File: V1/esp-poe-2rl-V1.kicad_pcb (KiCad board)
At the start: 2 copper layers, 88 x 45 mm, 94 parts, among them J1 USB_C_Receptacle_USB2.0, J2 RJ45 JACK, J3 1x2P 5,08mm, J4 1x2P 5,08mm, K1 G5NB-1A-E-DC5, K2 G5NB-1A-E-DC5, Q1 UMH3N, Q2 WPM2015-3/TR, Q3 LMUN2211LT1G, Q4 MMBT2222A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

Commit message: Prefab checks
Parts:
- D5, D7, D8: value GREEN -> EMERALD
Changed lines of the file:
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@@
 				(type "Bottom Solder Paste")
 			)
-			(layer "B.SilkS"
+			(layer "dielectric 2"
 				(type "Bottom Silk Screen")
+				(thickness 0)
+				(material "FR4")
+				(epsilon_r 4.5)
+				(loss_tangent 0.02)
 			)
 			(copper_finish "None")
@@
 			)
 		)
-		(property "Value" "GREEN"
+		(property "Value" "EMERALD"
 			(at 0 1.43 0)
 			(layer "F.Fab")
@@
 			)
 		)
-		(property "LCSC Part #" "C72043"
+		(property "LCSC Part #" "C2984266"
 			(at 0 0 0)
 			(layer "F.Fab")
@@
 			)
 		)
-		(property "Mfr" "Everlight"
+		(property "Mfr" "Everlight eLEC"
 			(at 0 0 0)
 			(layer "F.Fab")
@@
 			)
 		)
-		(property "Mfr PN" "19-217/GHC-YR1S2/3T"
+		(property "Mfr PN" "19-213/GHC-XS1T1/5T"
 			(at 0 0 0)
 			(layer "F.Fab")
@@
 			)
 		)
-		(property "Vendor PN" "C72043"
+		(property "Vendor PN" "C2984266"
 			(at 0 0 0)
 			(layer "F.Fab")
@@
 			)
 		)
-		(property "Value" "GREEN"
+		(property "Value" "EMERALD"
 			(at 0 1.43 0)
 			(layer "F.Fab")
@@
 			)
 		)
-		(property "LCSC Part #" "C72043"
+		(property "LCSC Part #" "C2984266"
 			(at 190.575 156 0)
 			(layer "F.Fab")
@@
 			)
 		)
-		(property "Mfr" "Everlight"
+		(property "Mfr" "Everlight eLEC"
 			(at 190.575 156 0)
 			(layer "F.Fab")
@@
 			)
 		)
-		(property "Mfr PN" "19-217/GHC-YR1S2/3T"
+		(property "Mfr PN" "19-213/GHC-XS1T1/5T"
 			(at 190.575 156 0)
 			(layer "F.Fab")
@@
 			)
 		)
-		(property "Vendor PN" "C72043"
+		(property "Vendor PN" "C2984266"
 			(at 190.575 156 0)
 			(layer "F.Fab")
@@
 			)
 		)
-		(property "Value" "GREEN"
+		(property "Value" "EMERALD"
 			(at 0 1.43 0)
 			(layer "F.Fab")
@@
 			)
 		)
-		(property "LCSC Part #" "C72043"
+		(property "LCSC Part #" "C2984266"
 			(at 164.575 156 0)
 			(layer "F.Fab")
@@
 			)
 		)
-		(property "Mfr" "Everlight"
+		(property "Mfr" "Everlight eLEC"
 			(at 164.575 156 0)
 			(layer "F.Fab")
@@
 			)
 		)
-		(property "Mfr PN" "19-217/GHC-YR1S2/3T"
+		(property "Mfr PN" "19-213/GHC-XS1T1/5T"
 			(at 164.575 156 0)
 			(layer "F.Fab")
@@
 			)
 		)
-		(property "Vendor PN" "C72043"
+		(property "Vendor PN" "C2984266"
 			(at 164.575 156 0)
 			(layer "F.Fab")

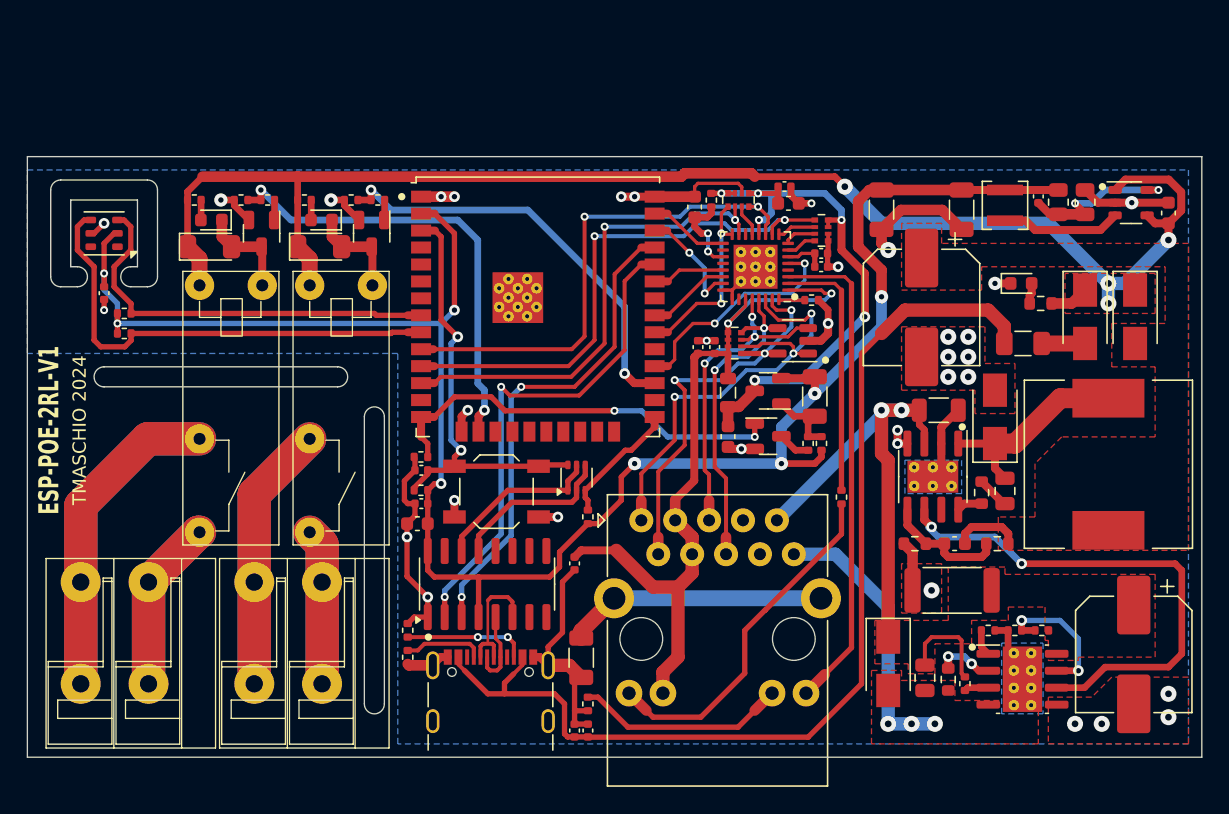
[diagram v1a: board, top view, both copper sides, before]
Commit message: Redoing routing because was too crapy
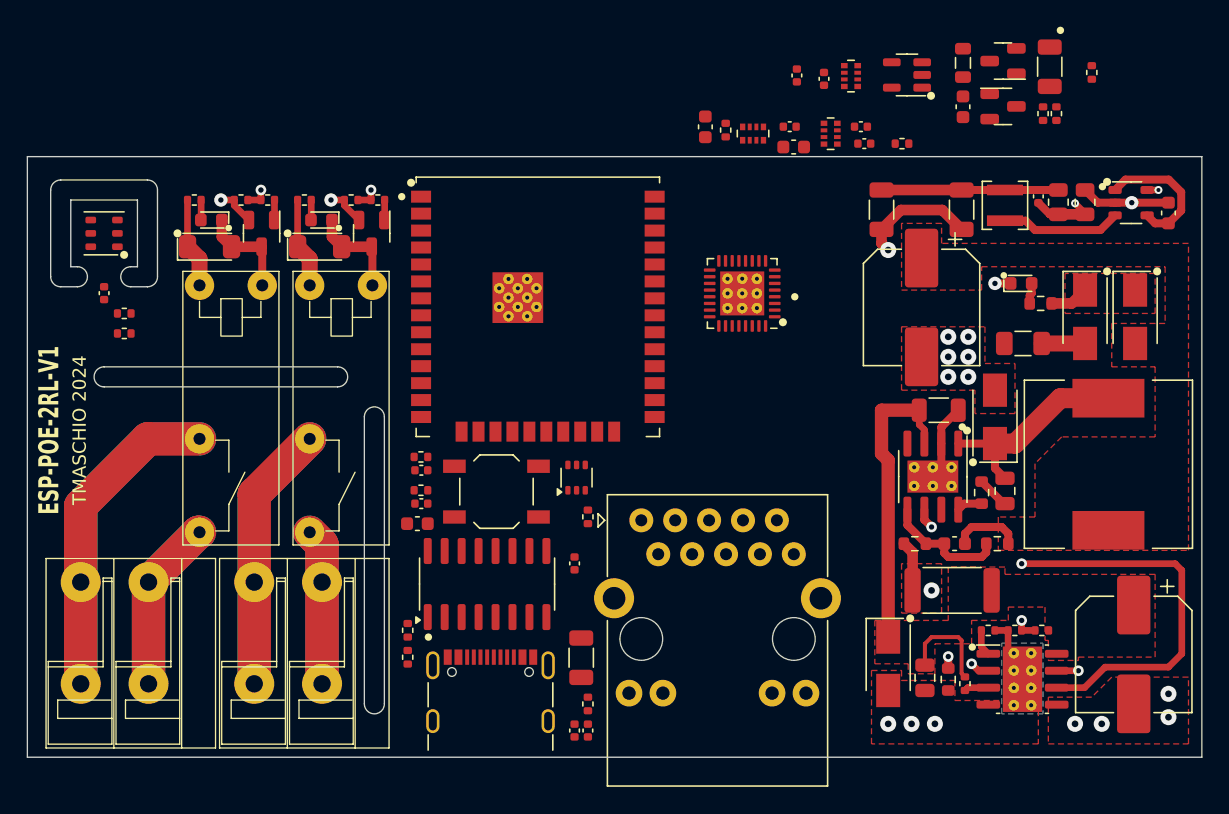
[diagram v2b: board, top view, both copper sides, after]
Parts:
- moved R21 36.9 mm to (155.8, 64.7)
- moved C24 30.3 mm to (152.6, 64.3)
- moved C25 30.3 mm to (146.1, 67.3)
- moved L3 30.3 mm to (146.1, 64.0)
- moved Q2 30.3 mm to (149.1, 63.8)
- moved Q3 30.3 mm to (149.1, 67.2)
- moved R23 30.3 mm to (153.1, 67.8)
- moved R24 30.3 mm to (152.1, 67.8)
- moved RN3 21.8 mm to (137.7, 65.0)
- moved C16 21.7 mm to (135.7, 65.2)
- moved D6 21.7 mm to (141.9, 64.9)
- moved C18 21.7 mm to (133.7, 64.9)
- moved R20 13.5 mm to (141.5, 70.0)
- moved C21 9.95 mm to (138.5, 68.8)
- moved C20 9.77 mm to (138.7, 70.0)
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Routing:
- net +3.3V: track 145.0 -> 13.2 mm, vias 8 -> 0
- net +5V: track 110.7 -> 26.7 mm, vias 4 -> 0
- net Net-(C10-Pad1): track 77.9 -> 0.00 mm
- net GND: track 100.1 -> 26.5 mm, vias 34 -> 16
- net +3.3VA: track 57.2 -> 0.00 mm, vias 2 -> 0
- net +3.3VLAN: track 43.7 -> 0.00 mm, vias 6 -> 0
- net /EMAC_RXD1: track 40.7 -> 0.00 mm, vias 2 -> 0
- net /EMAC_RXD0: track 38.1 -> 0.00 mm, vias 2 -> 0
- net Net-(U4-TXD): track 37.9 -> 0.00 mm, vias 2 -> 0
- net /LED_Y_A: track 37.1 -> 0.00 mm
- net Net-(U4-RXD): track 36.6 -> 0.00 mm, vias 2 -> 0
- net /EMAC_RX: track 36.3 -> 0.00 mm, vias 2 -> 0
- net I2C_SDA: track 35.7 -> 0.00 mm
- net /RD-: track 34.4 -> 0.00 mm, vias 3 -> 0
- net Net-(Q1A-C1): track 32.7 -> 0.00 mm, vias 2 -> 0
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- added copper zone on In1.Cu, net GND
- added copper zone on In1.Cu, net Net-(R7-Pad2)
- removed copper zone on B.Cu, net GND
- removed copper zone on B.Cu, net Net-(R7-Pad2)
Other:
- copper layers 2 -> 4

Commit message: Redoing routing
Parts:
- added R33: 22R/62,5mW, Tales:R_0402_1005Metric, F.Cu at (125.5, 86.5)
- moved RN3 29.5 mm to (134.5, 94.3), turned to 0 degrees
- moved RN2 14.5 mm to (133.3, 83.5), turned to 90 degrees
- moved RN1 14.2 mm to (130.3, 83.5)
- moved U6 7.65 mm to (131.1, 88.8)
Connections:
- U5 pad 28: /EMAC_CLK -> Net-(U5-IO17)
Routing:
- net /RD+: track 0.00 -> 17.9 mm, vias 0 -> 1
- net /RD-: track 0.00 -> 16.9 mm, vias 0 -> 3
- net /TD+: track 0.00 -> 15.1 mm, vias 0 -> 2
- net /TD-: track 0.00 -> 13.6 mm, vias 0 -> 2
- net /EMAC_MDIO: track 0.00 -> 6.57 mm
- net /EMAC_CLK: track 0.00 -> 4.21 mm
- net GND: track 26.5 -> 29.0 mm, vias 16 -> 18
- net +3.3VA: track 0.00 -> 1.56 mm
- net +3.3VLAN: track 0.00 -> 1.06 mm

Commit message: Update esp-poe-2rl-V1.kicad_pcb
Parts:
- moved R21 51.5 mm to (138.0, 113.0)
- moved D6 29.5 mm to (136.6, 94.0), turned to 0 degrees
- moved C16 28.3 mm to (126.8, 92.0), turned to 180 degrees
- moved C18 25.9 mm to (135.2, 90.8), turned to 0 degrees
- moved R20 22.6 mm to (135.3, 91.8)
- moved L3 21.5 mm to (128.0, 75.6), turned to -90 degrees
- moved C15 20.2 mm to (126.2, 89.0), turned to 0 degrees
- moved Q2 19.3 mm to (133.0, 74.5)
- moved Q3 19.1 mm to (133.0, 77.5)
- moved R22 19.0 mm to (137.0, 113.0), turned to 90 degrees
- moved R19 18.8 mm to (126.5, 87.8), turned to 180 degrees
- moved R23 18.7 mm to (135.5, 74.0), turned to -90 degrees
- moved R24 18.5 mm to (135.5, 76.0)
- moved C24 18.5 mm to (137.5, 75.0)
- moved C25 18.0 mm to (130.0, 75.3)
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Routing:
- net /LED_G_K: track 0.00 -> 28.1 mm, vias 0 -> 2
- net /LED_Y_A: track 0.00 -> 27.7 mm, vias 0 -> 1
- net /EMAC_CLK: track 4.21 -> 27.2 mm
- net PoE-: track 4.23 -> 26.5 mm
- net +3.3VA: track 1.56 -> 21.0 mm
- net Net-(J2-RLED-): track 0.00 -> 19.4 mm
- net Net-(J2-SHIELD): track 0.00 -> 15.5 mm
- net PoE+: track 30.2 -> 42.7 mm, vias 0 -> 3
- net /TD-: track 13.6 -> 25.5 mm, vias 2 -> 3
- net +3.3VLAN: track 1.06 -> 11.6 mm, vias 0 -> 3
- net /RD-: track 16.9 -> 24.0 mm, vias 3 -> 4
- net Net-(J2-LLED-): track 0.00 -> 6.15 mm
- net /RD+: track 17.9 -> 23.5 mm
- net /TD+: track 15.1 -> 20.6 mm
- net GND: track 29.0 -> 34.1 mm, vias 18 -> 21
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
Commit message: Redoing routing
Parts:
- SW1: footprint Tales:SW_SPST_TL3342 -> Tales:SW_SPST_Xunpu_TS1088AR02016
- moved C23 9.39 mm to (124.0, 95.2), turned to 180 degrees
- moved R17 9.19 mm to (124.8, 91.8)
- moved R15 9.01 mm to (113.5, 106.8), turned to 0 degrees
- moved R14 4.36 mm to (108.5, 106.8), turned to 180 degrees
- moved C12 2.85 mm to (106.0, 95.8)
- moved C13 2.50 mm to (105.5, 94.5)
- moved R16 2.50 mm to (107.5, 94.5), turned to 0 degrees
- moved C14 2.24 mm to (107.5, 93.5)
- moved C15 2.00 mm to (126.2, 87.0)
- moved C10 1.79 mm to (116.8, 112.2), turned to -90 degrees
- moved C11 1.79 mm to (117.8, 112.2), turned to -90 degrees
- moved SW1 1.39 mm to (112.0, 95.0), turned to 0 degrees
- moved U4 1.12 mm to (110.9, 102.0)
- moved R33 0.95 mm to (125.5, 85.8)
- moved R19 0.50 mm to (126.5, 88.2)
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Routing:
- net +3.3V: track 13.2 -> 89.5 mm, vias 0 -> 3
- net +3.3VA: track 21.0 -> 47.1 mm, vias 0 -> 1
- net Net-(C10-Pad1): track 0.00 -> 12.8 mm
- net Net-(Q1A-E1): track 0.00 -> 12.3 mm
- net Net-(Q1A-B1): track 0.00 -> 11.8 mm
- net GND: track 34.1 -> 39.4 mm
- net Net-(Q2-G): track 0.00 -> 4.91 mm
- net /USB_D-: track 0.00 -> 4.79 mm
- net /USB_D+: track 0.00 -> 4.47 mm
- net +3.3VLAN: track 11.6 -> 15.9 mm
- net /EMAC_TXD0: track 0.00 -> 3.83 mm, vias 0 -> 1
- net /EMAC_TXD1: track 0.00 -> 3.62 mm, vias 0 -> 1
- net PHY_PWR: track 0.00 -> 3.20 mm
- net Net-(Q1A-C1): track 0.00 -> 3.12 mm
- net Net-(U6-~{RST}): track 0.00 -> 2.88 mm
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
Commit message: Redoing routing
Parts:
- moved R32 20.7 mm to (104.0, 84.8), turned to 90 degrees
- moved R31 20.7 mm to (104.0, 82.5), turned to -90 degrees
- moved C22 8.82 mm to (117.8, 99.7), turned to 90 degrees
- moved R17 5.05 mm to (120.0, 93.5), turned to 0 degrees
- moved R22 4.00 mm to (137.0, 109.0)
- moved R21 1.41 mm to (137.0, 112.0)
- moved R33 1.10 mm to (124.5, 86.2), turned to 90 degrees
- moved C26 1.00 mm to (81.8, 80.2)
- moved R19 0.92 mm to (127.0, 87.5), turned to 90 degrees
- moved C16 0.68 mm to (127.2, 91.5), turned to 90 degrees
- moved C23 0.54 mm to (123.5, 95.2)
- moved C15 0.53 mm to (125.8, 87.2), turned to -90 degrees
- moved C19 0.50 mm to (134.3, 81.8)
- moved C24 0.50 mm to (137.5, 75.5)
- moved C25 0.50 mm to (130.0, 74.8)
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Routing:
- net +5V: track 26.7 -> 109.6 mm, vias 0 -> 2
- net Net-(C10-Pad1): track 12.8 -> 81.0 mm, vias 0 -> 2
- net +3.3V: track 89.5 -> 141.4 mm, vias 3 -> 8
- net PHY_PWR: track 3.20 -> 43.6 mm, vias 0 -> 3
- net Net-(U4-TXD): track 0.00 -> 34.5 mm, vias 0 -> 2
- net I2C_SDA: track 0.00 -> 33.3 mm
- net Net-(U4-RXD): track 0.00 -> 33.2 mm, vias 0 -> 2
- net I2C_SCL: track 0.00 -> 32.7 mm
- net Net-(Q1A-C1): track 3.12 -> 34.4 mm, vias 0 -> 2
- net /EMAC_RXD1: track 2.39 -> 32.0 mm, vias 0 -> 2
- net /EMAC_RXD0: track 2.62 -> 31.7 mm, vias 0 -> 2
- net OUT2: track 1.73 -> 30.3 mm, vias 1 -> 2
- net GND: track 39.4 -> 67.9 mm, vias 21 -> 40
- net OUT1: track 1.73 -> 28.8 mm, vias 1 -> 2
- net /EMAC_MDC: track 0.00 -> 26.5 mm, vias 0 -> 2
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- added copper zone on B.Cu, net GND
- added copper zone on In2.Cu, net GND
- added copper zone on B.Cu, net Net-(R7-Pad2)
- added copper zone on In2.Cu, net Net-(R7-Pad2)

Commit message: Routing redone
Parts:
- moved C26 2.25 mm to (81.8, 82.5)
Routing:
- net GND: track 67.9 -> 73.7 mm, vias 40 -> 41
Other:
- board text added: "5V OK"
- board text added: "OUT1"
- board text added: "OUT2"
- board text added: "PoE 802.3af"
- board text added: "RESET"
- board text added: "TMASCHIO 2025"
- board text removed: "TMASCHIO 2024"
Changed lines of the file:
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@@
 	(footprint "Tales:C_0402_1005Metric"
 		(layer "F.Cu")
-		(at 81.75 80.23 -90)
+		(at 81.75 82.48 -90)
 		(descr "Capacitor SMD 0402 (1005 Metric), square (rectangular) end terminal, IPC_7351 nominal, (Body size source: IPC-SM-782 page 76, https://www.pcb-3d.com/wordpress/wp-content/uploads/ipc-sm-782a_amendment_1_and_2.pdf), generated with kicad-footprint-generator")
 		(tags "capacitor")
@@
 	)
 	(gr_circle
-		(center 153.404 61.539)
-		(end 153.604 61.539)
-		(stroke
-			(width 0.15)
-			(type solid)
-		)
-		(fill solid)
-		(layer "F.SilkS")
-	)
-	(gr_circle
 		(center 146.8 107.75)
 		(end 147 107.75)
@@
 		(layer "Edge.Cuts")
 	)
-	(gr_text "TMASCHIO 2024"
+	(gr_text "OUT1"
+		(at 79.5 100 0)
+		(layer "F.SilkS")
+		(effects
+			(font
+				(size 1.1 0.9)
+				(thickness 0.15)
+			)
+		)
+	)
+	(gr_text "TMASCHIO 2025"
 		(at 80.5 91.5 90)
 		(layer "F.SilkS")
@@
 		)
 	)
+	(gr_text "5V OK"
+		(at 150.5 78.75 0)
+		(layer "F.SilkS")
+		(effects
+			(font
+				(size 1.1 0.9)
+				(thickness 0.15)
+			)
+		)
+	)
+	(gr_text "PoE 802.3af"
+		(at 136.5 115 0)
+		(layer "F.SilkS")
+		(effects
+			(font
+				(size 1.2 1)
+				(thickness 0.25)
+				(bold yes)
+			)
+			(justify left)
+		)
+	)
+	(gr_text "RESET"
+		(at 112 97 0)
+		(layer "F.SilkS")
+		(effects
+			(font
+				(size 1.1 0.9)
+				(thickness 0.15)
+			)
+		)
+	)
+	(gr_text "OUT2"
+		(at 104 103 90)
+		(layer "F.SilkS")
+		(effects
+			(font
+				(size 1.1 0.9)
+				(thickness 0.15)
+			)
+		)
+	)
 	(gr_text "ESP-POE-2RL-V1"
 		(at 78.5 91.5 90)
@@
 	)
 	(segment
-		(start 81.75 80.71)
-		(end 81.75 81.25)
+		(start 81.75 82.96)
+		(end 81.75 83.5)
 		(width 0.5)
 		(layer "F.Cu")
@@
 	)
 	(via
-		(at 81.75 81.25)
+		(at 81.75 83.5)
 		(size 0.6)
 		(drill 0.3)
@@
 	)
 	(via
+		(at 80 81.75)
+		(size 0.6)
+		(drill 0.3)
+		(layers "F.Cu" "B.Cu")
+		(net 3)
+	)
+	(via
 		(at 135.25 83)
 		(size 0.6)
@@
 	)
 	(segment
+		(start 81 77.75)
+		(end 81 80.75)
+		(width 0.4)
+		(layer "B.Cu")
+		(net 3)
+	)
+	(segment
+		(start 80 76.75)
+		(end 81 77.75)
+		(width 0.4)
+		(layer "B.Cu")
+		(net 3)
+	)
+	(segment
+		(start 81 80.75)
+		(end 80 81.75)
+		(width 0.4)
+		(layer "B.Cu")
+		(net 3)
+	)
+	(segment
 		(start 148.5 94.35)
 		(end 149.25 95.1)
@@
 	)
 	(segment
-		(start 81.75 79.75)
-		(end 81.75 79)
+		(start 81.75 82)
+		(end 81.75 81.25)
 		(width 0.4)
 		(layer "F.Cu")
@@
 	)
 	(via
-		(at 81.75 79)
+		(at 81.75 81.25)
 		(size 0.6)
 		(drill 0.3)
@@
 	)
 	(segment
-		(start 83 76.75)
-		(end 83.5 76.75)
-		(width 0.4)
-		(layer "In2.Cu")
-		(net 9)
-	)
-	(segment
-		(start 81.75 78)
-		(end 83 76.75)
-		(width 0.4)
-		(layer "In2.Cu")
-		(net 9)
-	)
-	(segment
-		(start 82.5 79.75)
-		(end 82.5 81)
-		(width 0.4)
-		(layer "In2.Cu")
-		(net 9)
-	)
-	(segment
 		(start 104 82.5)
 		(end 104 81.25)
@@
 	)
 	(segment
-		(start 104 84.105)
+		(start 83 82.5)
 		(end 104 82.5)
-		(width 0.5)
+		(width 0.4)
 		(layer "In2.Cu")
 		(net 9)
 	)
 	(segment
-		(start 81.75 79)
-		(end 81.75 78)
-		(width 0.4)
+		(start 104 84.105)
+		(end 104 82.5)
+		(width 0.5)
 		(layer "In2.Cu")
 		(net 9)
 	)
 	(segment
-		(start 82.5 81)
-		(end 84 82.5)
+		(start 81.75 78.5)
+		(end 83.5 76.75)
 		(width 0.4)
 		(layer "In2.Cu")
@@
 	)
 	(segment
-		(start 81.75 79)
-		(end 82.5 79.75)
+		(start 81.75 81.25)
+		(end 83 82.5)
 		(width 0.4)
 		(layer "In2.Cu")
@@
 	)
 	(segment
-		(start 103.25 84.855)
-		(end 104 84.105)
-		(width 0.5)
+		(start 81.75 81.25)
+		(end 81.75 78.5)
+		(width 0.4)
 		(layer "In2.Cu")
 		(net 9)
 	)
 	(segment
-		(start 84 82.5)
-		(end 104 82.5)
-		(width 0.4)
+		(start 103.25 84.855)
+		(end 104 84.105)
+		(width 0.5)
 		(layer "In2.Cu")
 		(net 9)
@@
 	)
 	(segment
-		(start 81 78.75)
-		(end 81.5 78.25)
+		(start 81.5 84.25)
+		(end 81 83.75)
 		(width 0.25)
 		(layer "F.Cu")
@@
 	)
 	(segment
-		(start 81.5 76)
-		(end 81.25 75.75)
+		(start 104 84.25)
+		(end 81.5 84.25)
 		(width 0.25)
 		(layer "F.Cu")
@@
 	)
 	(segment
-		(start 81.75 84.25)
-		(end 81 83.5)
+		(start 81.5 76)
+		(end 81.25 75.75)
 		(width 0.25)
 		(layer "F.Cu")
@@
 	)
 	(segment
-		(start 81 83.5)
-		(end 81 78.75)
+		(start 81 78.75)
+		(end 81.5 78.25)
 		(width 0.25)
 		(layer "F.Cu")
@@
 	)
 	(segment
-		(start 104 84.25)
-		(end 105.41 84.25)
-		(width 0.6)
-		(layer "F.Cu")
-		(net 106)
-	)
-	(segment
 		(start 81.25 75.75)
 		(end 80.75 75.75)
@@
 	(segment
 		(start 104 84.25)
-		(end 81.75 84.25)
+		(end 105.41 84.25)
+		(width 0.6)
+		(layer "F.Cu")
+		(net 106)
+	)
+	(segment
+		(start 81 83.75)
+		(end 81 78.75)
 		(width 0.25)
 		(layer "F.Cu")
@@
 			)
 		)
+	)
+	(zone
+		(net 0)
+		(net_name "")
+		(layers "F.Cu" "In1.Cu" "In2.Cu" "B.Cu")
+		(hatch edge 0.5)
+		(connect_pads
+			(clearance 0)
+		)
+		(min_thickness 0.25)
+		(filled_areas_thickness no)
+		(keepout
+			(tracks allowed)
+			(vias allowed)
+			(pads allowed)
+			(copperpour not_allowed)
+			(footprints allowed)
+		)
+		(fill
+			(thermal_gap 0.5)
+			(thermal_bridge_width 0.5)
+		)
+		(polygon
+			(pts
+				(xy 79.25 74.25) (xy 84.25 74.25) (xy 84.25 81) (xy 79.25 81)
+			)
+		)

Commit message: Files for release 1.3.0
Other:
- board text added: "ESP-POE-2RL V1.3"
- board text removed: "ESP-POE-2RL-V1"
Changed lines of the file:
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@@
 	)
 	(paper "A4")
+	(title_block
+		(title "ESP 2x Relay Output Module with PoE")
+		(date "2025-06-29")
+		(rev "V1.3")
+	)
 	(layers
 		(0 "F.Cu" signal)
@@
 		(layer "F.Cu")
 		(at 117.15 94.55 90)
-		(descr "SOT-363, SC-70-6")
-		(tags "SOT-363 SC-70-6")
+		(descr "SOT-363, SC-70-6, SC-88")
+		(tags "SOT-363 SC-70-6 SC-88")
 		(property "Reference" "Q1"
 			(at 0 -2.25 90)
@@
 	)
 	(gr_text "TMASCHIO 2025"
-		(at 80.5 91.5 90)
+		(at 80.5 90.5 90)
 		(layer "F.SilkS")
 		(effects
@@
 		)
 	)
-	(gr_text "ESP-POE-2RL-V1"
-		(at 78.5 91.5 90)
+	(gr_text "ESP-POE-2RL V1.3"
+		(at 78.5 90.5 90)
 		(layer "F.SilkS")
 		(effects
